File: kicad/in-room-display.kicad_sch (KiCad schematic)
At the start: 3 parts, among them J1 USBCpow, J2 Display, U1 ESP32-DevKitC

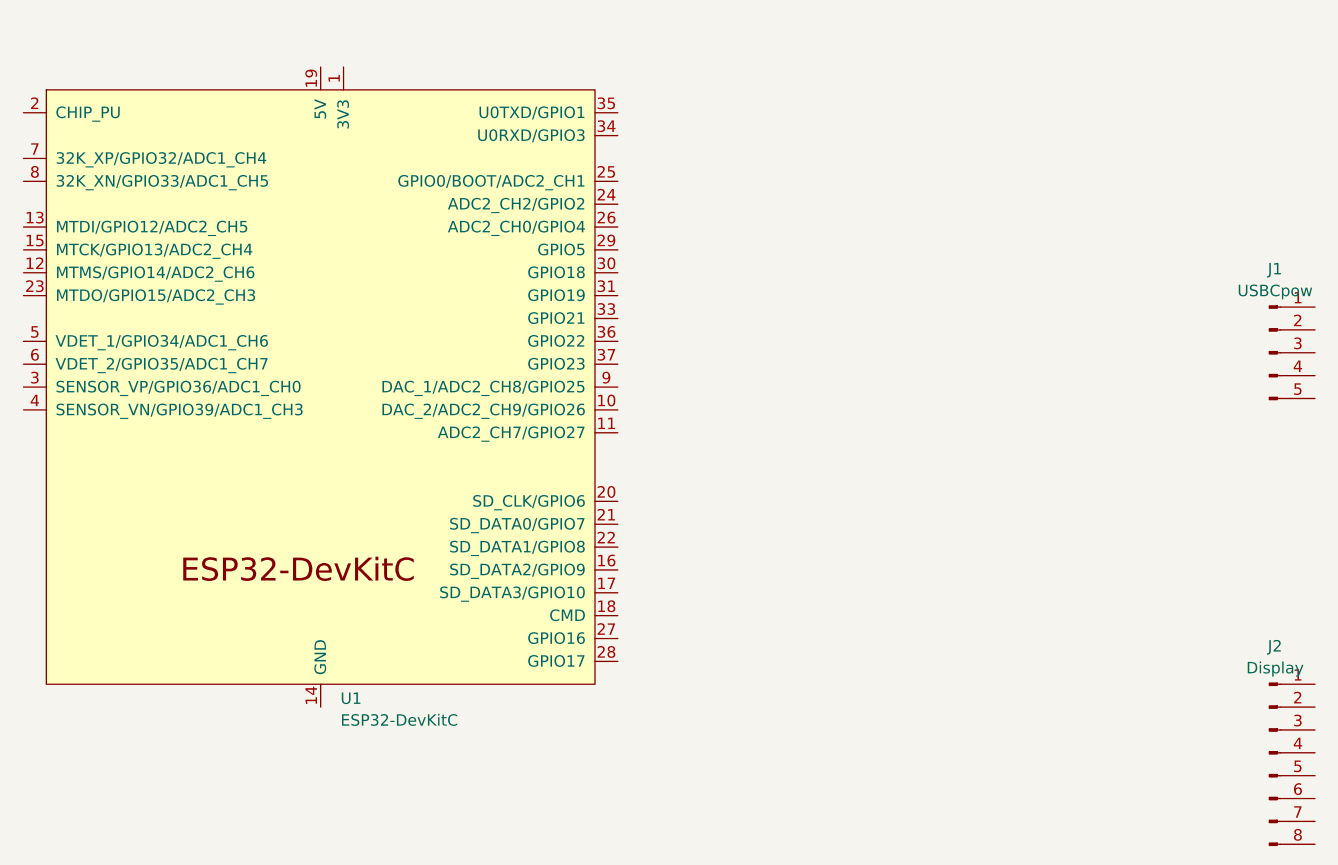
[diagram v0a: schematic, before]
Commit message: create pcb layout
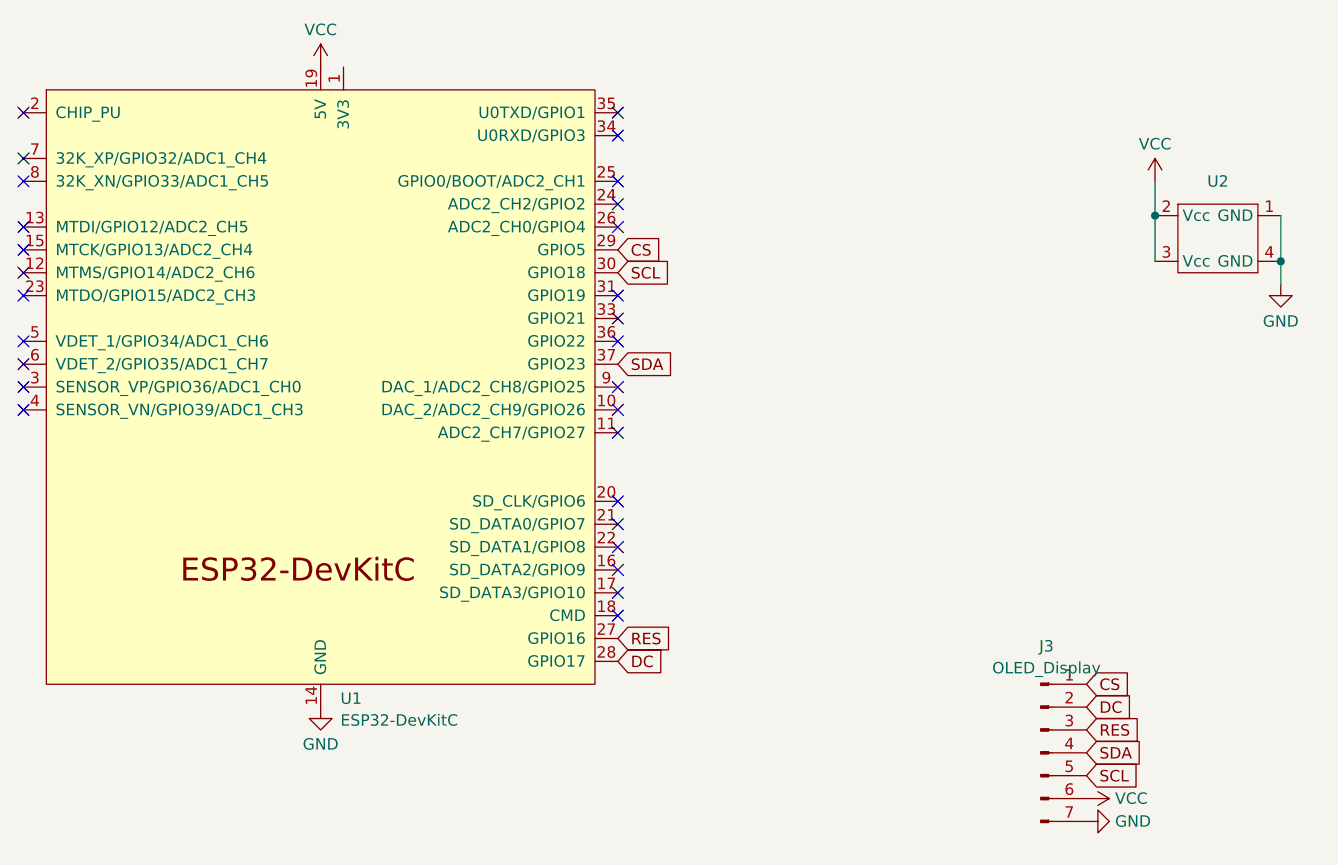
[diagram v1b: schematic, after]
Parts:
- removed J1: USBCpow, symbol Connector:Conn_01x05_Pin
- removed J2: Display, symbol Connector:Conn_01x08_Pin
- added J3: OLED_Display, Connector_PinHeader_2.54mm:PinHeader_1x07_P2.54mm_Vertical, symbol Connector:Conn_01x07_Pin
- added U2: ~, in-room-display:DIP-4_300_ELL, symbol in-room-display:pow-microusb
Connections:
- net GND: now reaches U1.14 (GND), U1.32 (GND), U1.38 (GND)
- net GND: now also J3.7 (Pin_7), U2.1 (GND), U2.4 (GND)
- net VCC: now reaches U1.19 (5V)
- net VCC: now also J3.6 (Pin_6), U2.2 (Vcc), U2.3 (Vcc)
- net RES: now reaches U1.27 (GPIO16)
- net RES: now also J3.3 (Pin_3)
- net DC: now reaches U1.28 (GPIO17)
- net DC: now also J3.2 (Pin_2)
- net CS: now reaches U1.29 (GPIO5)
- net CS: now also J3.1 (Pin_1)
- net SCL: now reaches U1.30 (GPIO18)
- net SCL: now also J3.5 (Pin_5)
- net SDA: now reaches U1.37 (GPIO23)
- net SDA: now also J3.4 (Pin_4)
- no-connect marks 0 -> 28
